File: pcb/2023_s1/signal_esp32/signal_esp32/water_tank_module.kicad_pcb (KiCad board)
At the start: 2 copper layers, 13 parts, among them J1 Conn_01x05_Male, J2 Conn_01x02_Male, U4 NRF24L01_Breakout

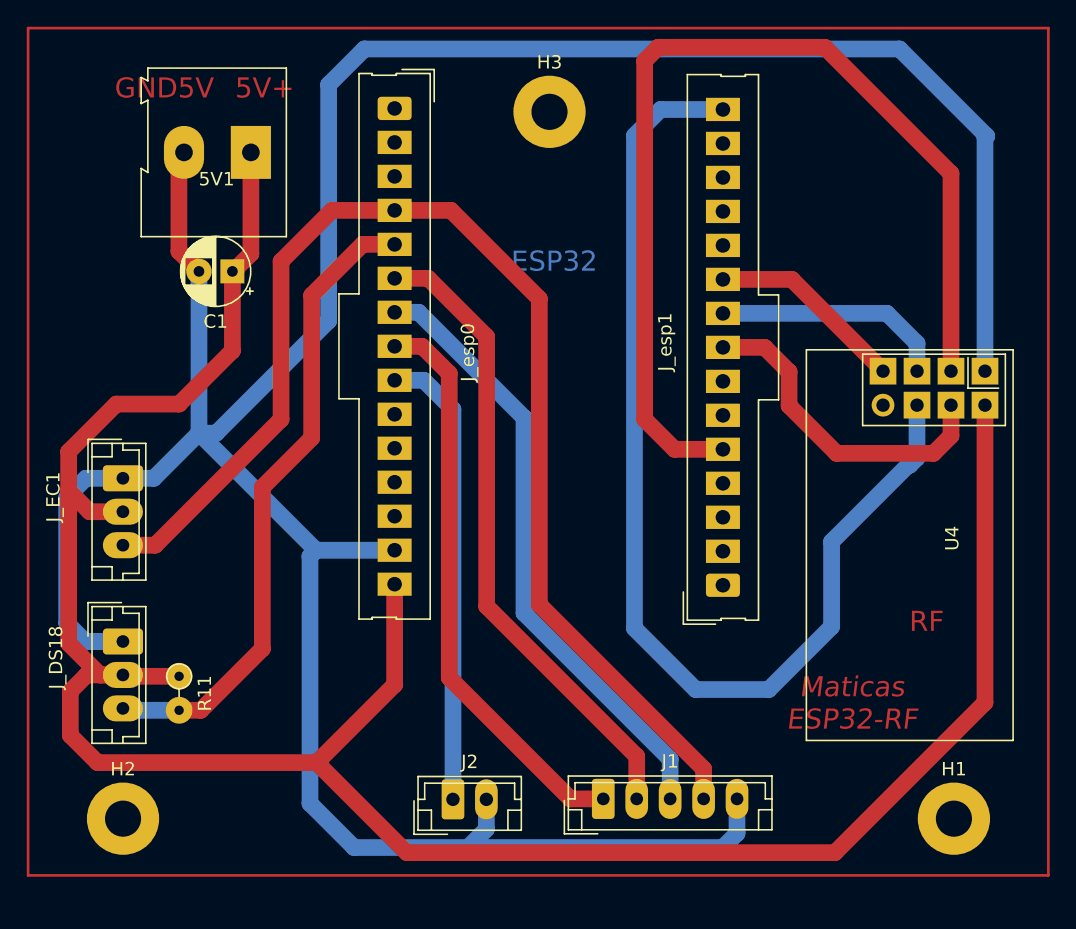
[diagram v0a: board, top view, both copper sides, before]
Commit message: fix, added a 4th mounting hole and rerouted the pcb in order to make feasible to solder given our poor infrastructure for PCB production
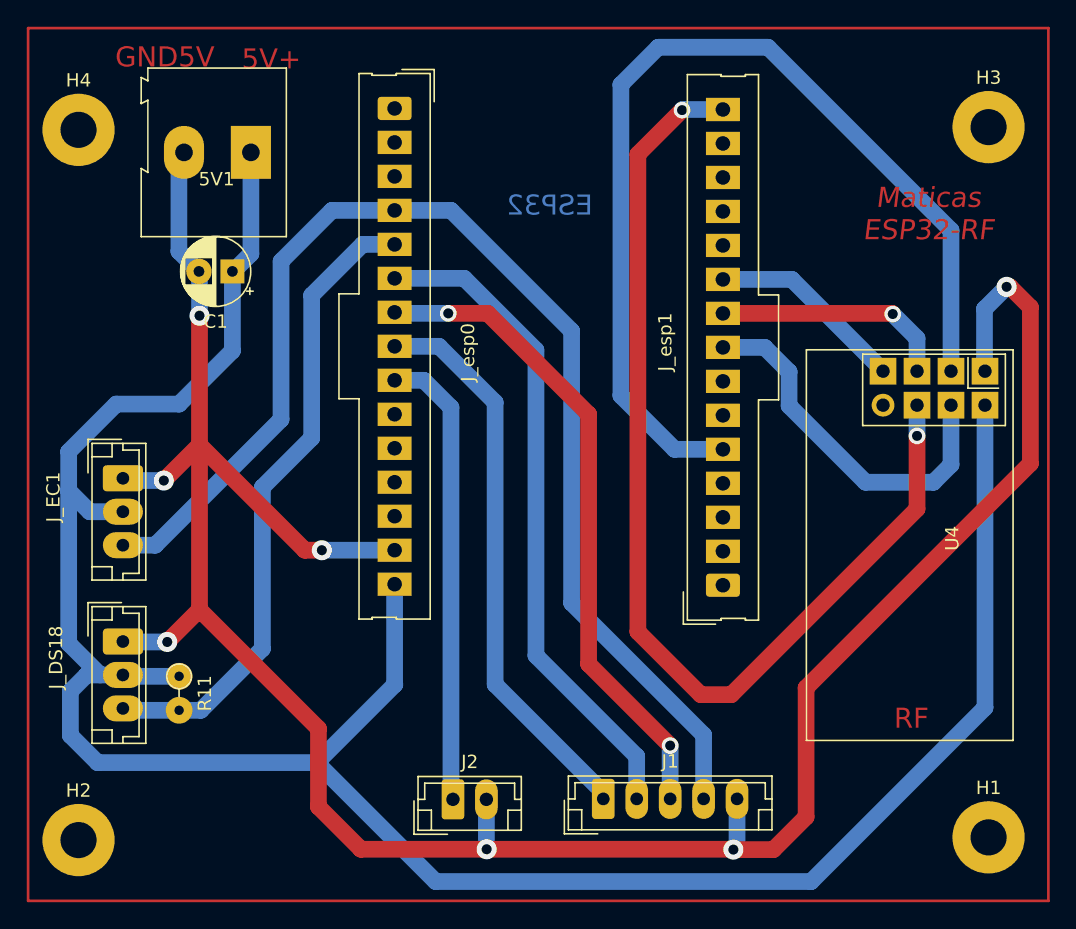
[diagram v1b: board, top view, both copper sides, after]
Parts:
- added H4: MountingHole, MountingHole:MountingHole_2.7mm_M2.5_Pad, F.Cu at (61.6, 28.9)
- moved H3 32.8 mm to (129.6, 28.7)
- moved H2 3.69 mm to (61.6, 82.0)
- moved H1 2.94 mm to (129.6, 81.8)
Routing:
- net GND5V: track 229.1 -> 185.9 mm, vias 0 -> 7
- net D5: track 24.7 -> 27.7 mm
- net D33: track 46.0 -> 48.9 mm, vias 0 -> 2
- net D23: track 82.1 -> 79.7 mm, vias 0 -> 2
- net D32: track 47.9 -> 49.5 mm
- net D4: track 75.6 -> 74.6 mm
- net D25: track 42.9 -> 42.2 mm
- net D18: track 17.5 -> 17.7 mm, vias 0 -> 1

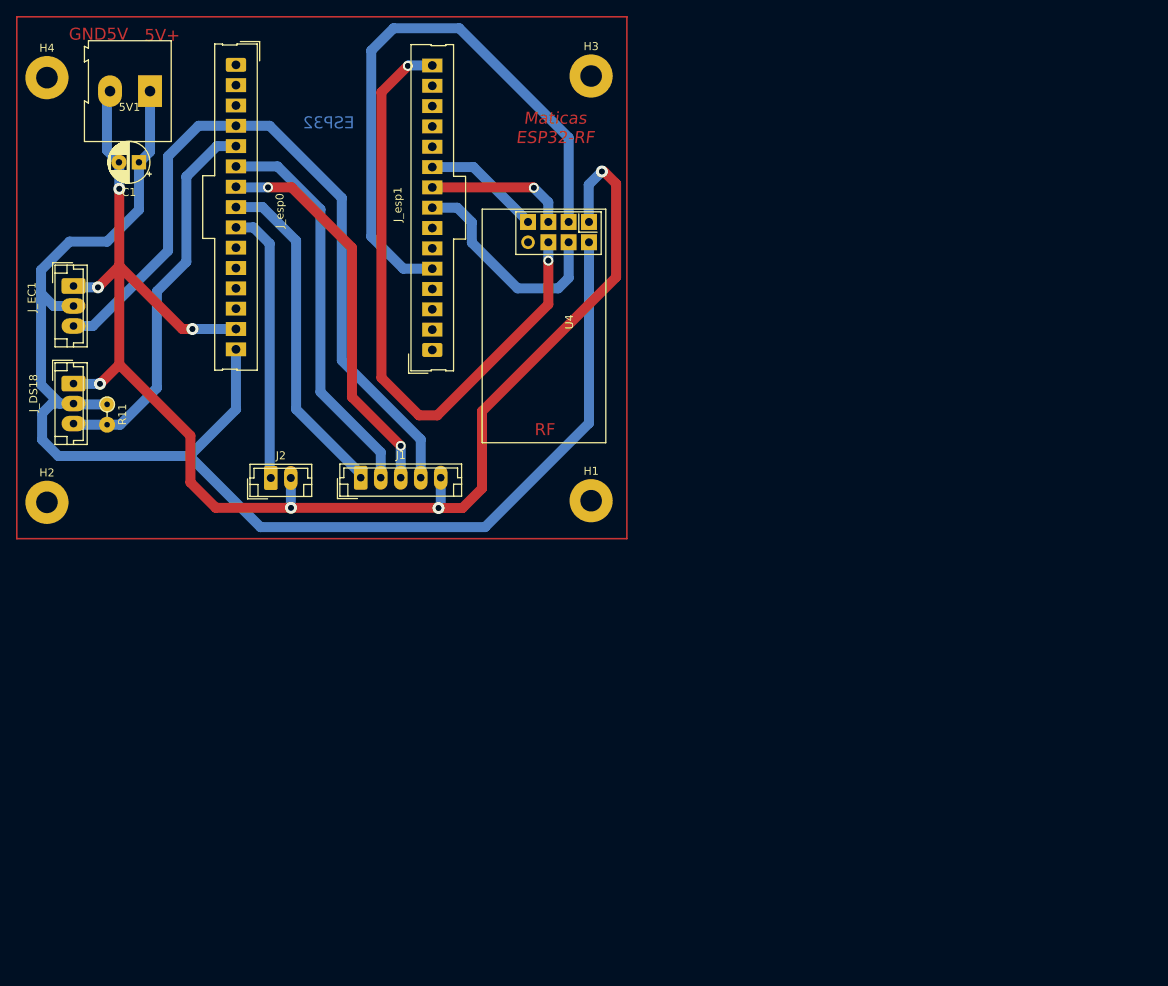
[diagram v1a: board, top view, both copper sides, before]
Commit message: update, reselection of output pins and ds18b20 pin, rerouting and resizing of pads
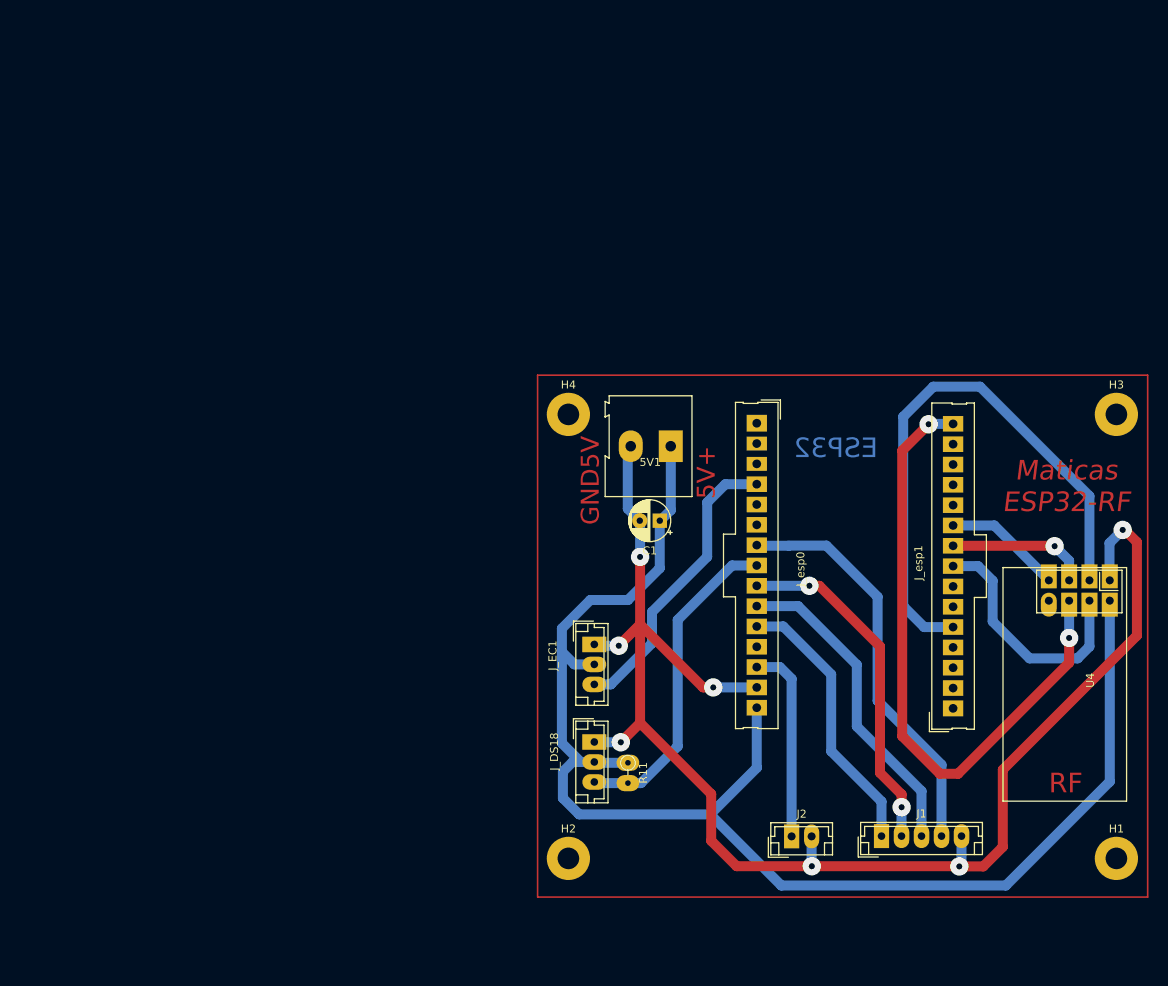
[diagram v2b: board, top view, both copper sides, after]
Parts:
- moved H1 79.4 mm to (195.2, 126.5)
- moved C1 79.0 mm to (138.2, 84.3)
- moved J1 79.0 mm to (165.9, 123.7)
- moved J2 79.0 mm to (154.7, 123.7)
- moved J_DS18 79.0 mm to (130.0, 111.9)
- moved J_EC1 79.0 mm to (130.0, 99.7)
- moved J_esp0 79.0 mm to (158.4, 90.3)
- moved J_esp1 79.0 mm to (166.7, 89.5)
- moved R11 79.0 mm to (134.2, 114.5)
- moved U4 79.0 mm to (194.4, 91.7)
- moved H2 78.9 mm to (126.8, 126.5)
- moved 5V1 78.8 mm to (139.5, 75.0)
- moved H3 78.1 mm to (195.2, 71.0)
- moved H4 77.6 mm to (126.8, 71.0)
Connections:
- J1 pad 1: D25 -> D14
- J1 pad 2: D32 -> D26
- J1 pad 3: D33 -> D27
- J1 pad 4: D34 -> D33
- J2 pad 1: D26 -> D13
- J_DS18 pad 3: D35 -> D25
- R11 pad 2: D35 -> D25
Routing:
- net D34: track 93.6 -> 36.9 mm
- net D32: track 49.5 -> 0.00 mm
- net D35: track 48.3 -> 0.00 mm
- net D27: track 0.00 -> 40.3 mm
- net D14: track 0.00 -> 34.6 mm
- net D13: track 0.00 -> 25.1 mm
- net D26: track 34.6 -> 43.4 mm, vias 0 -> 2
- net D5: track 27.7 -> 31.2 mm
- net D4: track 74.6 -> 72.0 mm
- net D33: track 48.9 -> 51.0 mm, vias 2 -> 0
- net D25: track 42.2 -> 41.1 mm
- net GND5V: track 185.9 -> 186.8 mm

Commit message: update, added aditional notation and repositioned components for better soldering
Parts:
- moved H1 3.50 mm to (195.2, 130.0)
- moved H2 3.50 mm to (126.8, 130.0)
- moved R11 0.31 mm to (134.5, 114.5)
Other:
- board text added: "-"
- board text added: "13"
- board text added: "14"
- board text added: "26"
- board text added: "27"
- board text added: "33"
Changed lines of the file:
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@@
   )
   (footprint "MountingHole:MountingHole_2.7mm_M2.5_Pad" (layer "F.Cu")
-    (at 126.75 126.5)
+    (at 126.75 130)
     (descr "Mounting Hole 2.7mm, M2.5")
     (tags "mounting hole 2.7mm m2.5")
@@
     (fp_line (start -0.633605 -1.3375) (end -0.633605 -0.8375) (layer "F.Fab") (width 0.1))
     (fp_circle (center 1.25 0) (end 3.75 0) (layer "F.Fab") (width 0.1) (fill none))
-    (pad "1" thru_hole rect (at 0 0 180) (size 1.8 1.8) (drill 0.8) (layers *.Cu *.Mask)
+    (pad "1" thru_hole rect (at 0 0 180) (size 3 2.5) (drill 0.8 (offset -0.6 0)) (layers *.Cu *.Mask)
       (net 29 "5v") (pintype "passive"))
-    (pad "2" thru_hole circle (at 2.5 0 180) (size 1.9 1.9) (drill 0.8) (layers *.Cu *.Mask)
+    (pad "2" thru_hole oval locked (at 2.5 0 180) (size 3 2.5) (drill 0.8 (offset 0.45 0)) (layers *.Cu *.Mask)
       (net 30 "GND5V") (pintype "passive"))
     (model "${KICAD6_3DMODEL_DIR}/Capacitor_THT.3dshapes/CP_Radial_D5.0mm_P2.50mm.wrl"
@@
   )
   (footprint "MountingHole:MountingHole_2.7mm_M2.5_Pad" (layer "F.Cu")
-    (at 195.25 126.5)
+    (at 195.25 130)
     (descr "Mounting Hole 2.7mm, M2.5")
     (tags "mounting hole 2.7mm m2.5")
@@
   )
   (footprint "Resistor_THT:R_Axial_DIN0204_L3.6mm_D1.6mm_P2.54mm_Vertical" (layer "F.Cu")
-    (at 134.188 114.54975 -90)
+    (at 134.5 114.54975 -90)
     (descr "Resistor, Axial_DIN0204 series, Axial, Vertical, pin pitch=2.54mm, 0.167W, length*diameter=3.6*1.6mm^2, http://cdn-reichelt.de/documents/datenblatt/B400/1_4W%23YAG.pdf")
     (tags "Resistor Axial_DIN0204 series Axial Vertical pin pitch 2.54mm 0.167W length 3.6mm diameter 1.6mm")
@@
     )
   )
-  (gr_rect (start 199.16 66.1) (end 122.9 131.335) (layer "F.Cu") (width 0.2) (fill none))
+  (gr_rect (start 199.16 66.1) (end 122.9 135.085) (layer "F.Cu") (width 0.2) (fill none))
+  (gr_text "13" (at 154.5 131.5 90) (layer "F.Cu")
+    (effects (font (size 2.45 2.45) (thickness 0.3)))
+  )
+  (gr_text "14" (at 165.5 132 90) (layer "F.Cu")
+    (effects (font (size 2.45 2.45) (thickness 0.3)))
+  )
   (gr_text "GND5V" (at 129.5 79.25 90) (layer "F.Cu")
     (effects (font (size 2.25 2.25) (thickness 0.3)))
   )
+  (gr_text "26" (at 169 132 90) (layer "F.Cu")
+    (effects (font (size 2.45 2.45) (thickness 0.3)))
+  )
+  (gr_text "33" (at 176 132 90) (layer "F.Cu")
+    (effects (font (size 2.45 2.45) (thickness 0.3)))
+  )
+  (gr_text "-" (at 179.5 131.999999) (layer "F.Cu")
+    (effects (font (size 2.45 2.45) (thickness 0.3)))
+  )
+  (gr_text "27" (at 172.5 132 90) (layer "F.Cu")
+    (effects (font (size 2.45 2.45) (thickness 0.3)))
+  )
   (gr_text "5V+" (at 144 78.25 90) (layer "F.Cu")
     (effects (font (size 2.25 2.25) (thickness 0.3)))
+  )
+  (gr_text "-" (at 157.5 131.499999) (layer "F.Cu")
+    (effects (font (size 2.45 2.45) (thickness 0.3)))
+  )
+  (gr_text "5V+\n" (at 157.25 107.75) (layer "F.Cu")
+    (effects (font (size 2.45 2.45) (thickness 0.3)))
   )
   (gr_text "RF" (at 188.925 117.1) (layer "F.Cu")
@@
   (segment (start 150.3712 87.4212) (end 150.295 87.345) (width 1.25) (layer "B.Cu") (net 7))
   (segment (start 130.128 117.08975) (end 129.988 116.94975) (width 1.25) (layer "F.Cu") (net 8))
-  (segment (start 130.128 117.08975) (end 129.988 116.94975) (width 1.25) (layer "B.Cu") (net 8))
-  (segment (start 134.188 117.08975) (end 130.128 117.08975) (width 1.25) (layer "B.Cu") (net 8))
-  (segment (start 134.188 117.08975) (end 135.81225 117.08975) (width 1.25) (layer "B.Cu") (net 8))
   (segment (start 140.411 112.491) (end 140.411 96.689) (width 1.25) (layer "B.Cu") (net 8))
   (segment (start 147.215 89.885) (end 150.295 89.885) (width 1.25) (layer "B.Cu") (net 8))
   (segment (start 135.81225 117.08975) (end 140.411 112.491) (width 1.25) (layer "B.Cu") (net 8))
+  (segment (start 130.128 117.08975) (end 135.81225 117.08975) (width 1.25) (layer "B.Cu") (net 8))
   (segment (start 140.411 96.689) (end 147.215 89.885) (width 1.25) (layer "B.Cu") (net 8))
+  (segment (start 129.988 116.94975) (end 130.128 117.08975) (width 1.25) (layer "B.Cu") (net 8))
   (segment (start 165.7 100) (end 165.7 115.8) (width 1.25) (layer "F.Cu") (net 9))
   (segment (start 165.7 115.8) (end 168.4 118.5) (width 1.25) (layer "F.Cu") (net 9))
@@
   (segment (start 129.988 102.24975) (end 127.50275 102.24975) (width 1.25) (layer "B.Cu") (net 29))
   (segment (start 125.933 100.68) (end 125.933 112.09475) (width 1.25) (layer "B.Cu") (net 29))
-  (segment (start 133.299 111.983) (end 135.712 109.57) (width 1.25) (layer "F.Cu") (net 30))
   (segment (start 178.6126 127.5024) (end 181.051 125.064) (width 1.25) (layer "F.Cu") (net 30))
   (segment (start 144.602 124.302) (end 144.602 118.46) (width 1.25) (layer "F.Cu") (net 30))
   (segment (start 175.6154 127.5024) (end 175.59 127.477) (width 1.25) (layer "F.Cu") (net 30))
   (segment (start 135.712 109.57) (end 135.712 97.251) (width 1.25) (layer "F.Cu") (net 30))
+  (segment (start 134.3565 98.6065) (end 135.712 97.251) (width 1.25) (layer "F.Cu") (net 30))
   (segment (start 197.815 98.648) (end 197.815 86.964) (width 1.25) (layer "F.Cu") (net 30))
   (segment (start 135.712 97.251) (end 135.712 88.812) (width 1.25) (layer "F.Cu") (net 30))
+  (segment (start 134.391 110.891) (end 135.712 109.57) (width 1.25) (layer "F.Cu") (net 30))
   (segment (start 144.856 105.125) (end 143.586 105.125) (width 1.25) (layer "F.Cu") (net 30))
   (segment (start 157.175 127.477) (end 147.777 127.477) (width 1.25) (layer "F.Cu") (net 30))
@@
   (segment (start 196.291 85.44) (end 196.037 85.44) (width 1.25) (layer "F.Cu") (net 30))
   (segment (start 143.586 105.125) (end 135.712 97.251) (width 1.25) (layer "F.Cu") (net 30))
-  (segment (start 133.045 99.918) (end 135.712 97.251) (width 1.25) (layer "F.Cu") (net 30))
   (segment (start 181.051 115.412) (end 197.815 98.648) (width 1.25) (layer "F.Cu") (net 30))
   (segment (start 175.6154 127.5024) (end 178.6126 127.5024) (width 1.25) (layer "F.Cu") (net 30))
@@
   (segment (start 144.602 118.46) (end 135.712 109.57) (width 1.25) (layer "F.Cu") (net 30))
   (segment (start 197.815 86.964) (end 196.291 85.44) (width 1.25) (layer "F.Cu") (net 30))
-  (via (at 133.045 99.918) (size 2.3) (drill 0.75) (layers "F.Cu" "B.Cu") (free) (net 30))
+  (via (at 134.3565 98.6065) (size 2.3) (drill 0.75) (layers "F.Cu" "B.Cu") (free) (net 30))
   (via (at 135.712 88.812) (size 2.3) (drill 0.75) (layers "F.Cu" "B.Cu") (free) (net 30))
   (via (at 175.6154 127.5024) (size 2.3) (drill 0.75) (layers "F.Cu" "B.Cu") (free) (net 30))
   (via (at 196.037 85.44) (size 2.3) (drill 0.75) (layers "F.Cu" "B.Cu") (free) (net 30))
   (via (at 144.856 105.125) (size 2.3) (drill 0.75) (layers "F.Cu" "B.Cu") (free) (net 30))
-  (via (at 133.299 111.983) (size 2.3) (drill 0.75) (layers "F.Cu" "B.Cu") (free) (net 30))
+  (via (at 134.391 110.891) (size 2.3) (drill 0.75) (layers "F.Cu" "B.Cu") (free) (net 30))
   (via (at 157.175 127.477) (size 2.3) (drill 0.75) (layers "F.Cu" "B.Cu") (free) (net 30))
   (segment (start 175.6154 127.5024) (end 175.891 127.2268) (width 1.25) (layer "B.Cu") (net 30))
-  (segment (start 133.299 111.983) (end 130.02125 111.983) (width 1.25) (layer "B.Cu") (net 30))
   (segment (start 175.891 127.2268) (end 175.891 123.713) (width 1.25) (layer "B.Cu") (net 30))
   (segment (start 157.155 127.457) (end 157.175 127.477) (width 1.25) (layer "B.Cu") (net 30))
   (segment (start 175.971 123.633) (end 175.891 123.713) (width 1.25) (layer "B.Cu") (net 30))
+  (segment (start 134.391 110.891) (end 133.299 111.983) (width 1.25) (layer "B.Cu") (net 30))
+  (segment (start 130.02125 111.983) (end 129.988 111.94975) (width 1.25) (layer "B.Cu") (net 30))
+  (segment (start 133.299 111.983) (end 130.02125 111.983) (width 1.25) (layer "B.Cu") (net 30))
   (segment (start 134.172 82.787137) (end 134.172 75.347) (width 1.25) (layer "B.Cu") (net 30))
-  (segment (start 130.02125 111.983) (end 129.988 111.94975) (width 1.25) (layer "B.Cu") (net 30))
+  (segment (start 134.3565 98.6065) (end 133.21325 99.74975) (width 1.25) (layer "B.Cu") (net 30))
   (segment (start 196.037 85.44) (end 194.386 87.091) (width 1.25) (layer "B.Cu") (net 30))
-  (segment (start 130.15625 99.918) (end 129.988 99.74975) (width 1.25) (layer "B.Cu") (net 30))
   (segment (start 144.856 105.125) (end 150.295 105.125) (width 1.25) (layer "B.Cu") (net 30))
   (segment (start 135.671113 84.28625) (end 134.172 82.787137) (width 1.25) (layer "B.Cu") (net 30))
   (segment (start 194.386 91.707) (end 194.423 91.744) (width 1.25) (layer "B.Cu") (net 30))
-  (segment (start 133.045 99.918) (end 130.15625 99.918) (width 1.25) (layer "B.Cu") (net 30))
   (segment (start 134.172 75.347) (end 134.5438 74.9752) (width 1.25) (layer "B.Cu") (net 30))
+  (segment (start 133.21325 99.74975) (end 129.988 99.74975) (width 1.25) (layer "B.Cu") (net 30))
   (segment (start 135.712 88.812) (end 135.712 84.327137) (width 1.25) (layer "B.Cu") (net 30))
   (segment (start 194.386 87.091) (end 194.386 91.707) (width 1.25) (layer "B.Cu") (net 30))
